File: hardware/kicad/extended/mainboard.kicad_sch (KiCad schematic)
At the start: 83 parts, among them J1 XT60PB-M vertical, J10 Body NeoPixel, J11 Slip ring (body lights), J13 SPK L, J14 SPK R, J15 ESTOP, J17 I2C-B exp (RP2350), J2 DFR0601 ribbon 2x5, J3 DFR0601 ribbon 2x5, J4 Servo L, J5 Servo R, J6 IMU BMI160 I2C, J7 S2S AS5600/pot, J8 Dome encoder, J9 Hall, Q1 Si7461DP P-FET RPP, U3 DFPlayer Mini, U5 AP7361C-33 3.3V LDO, U6 74AHCT125, U7 74LVC245A

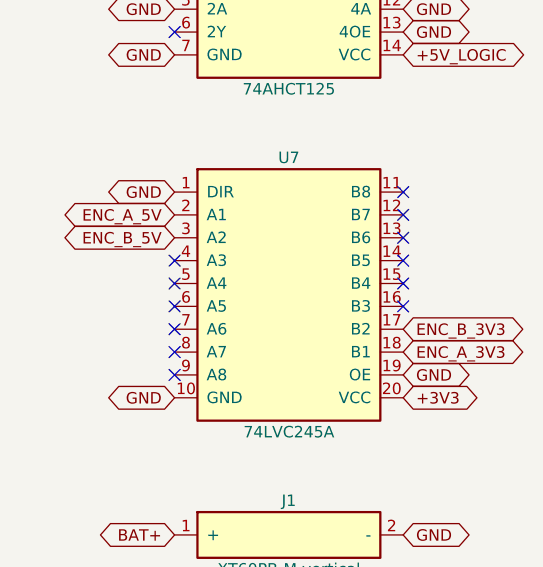
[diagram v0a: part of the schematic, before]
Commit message: v10 mainboard r7: fix U7 74LVC245 direction (DIR -> +3V3, A->B), tie unused A3..A8 to GND
DIR was strapped to GND, which per the SN74LVC245A pin table is B->A: the 5 V dome
encoder on A1/A2 would never reach the RP2350 on B1/B2 and U7's A outputs would fight
the encoder. Pad 1 is now +3V3 via a 0.2 mm jumper around the package end to pin 20;
A3..A8 (inputs once DIR=H) run along the row to pin 10 GND. Compact board still
0 DRC errors (17 warnings, 2 cosmetic zone-island lines). Extended board synced.
Regenerated both schematics (compact's was stale) and the JLCPCB package
(ZDrive_v10_compact_*_r7.zip; BOM/CPL unchanged from the r6 upload).

Rev-A boards built from r6 gerbers: cut the GND spoke into U7 pin 1 and bridge pin 1
to pin 20.

Co-Authored-By: Claude Fable 5 <noreply@anthropic.com>
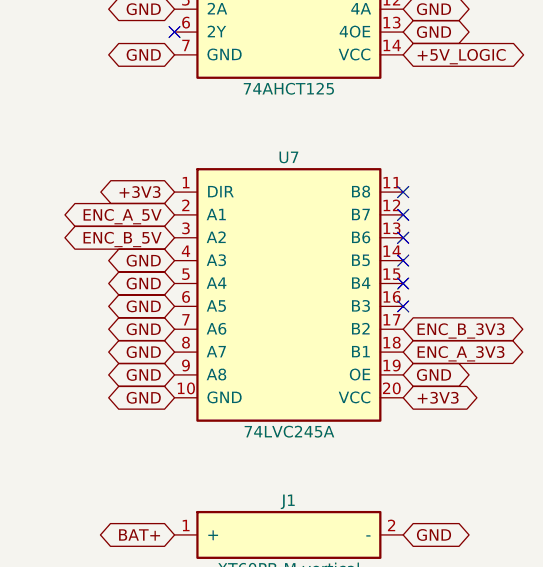
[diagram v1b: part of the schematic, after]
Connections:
- net +3V3: now also U7.1 (DIR)
- net GND: now also U7.4 (A3), U7.5 (A4), U7.6 (A5), U7.7 (A6), U7.8 (A7), U7.9 (A8); no longer U7.1 (DIR)
- no-connect marks 39 -> 33
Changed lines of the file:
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@@
     (instances (project "mainboard" (path "/0b82c761-6368-5a59-877e-dce7a78c7d89" (reference "U7") (unit 1))))
   )
-  (global_label "GND" (shape bidirectional) (at 59.69 207.01 180) (fields_autoplaced yes) (effects (font (size 1.27 1.27)) (justify right)) (property "Intersheetrefs" "${INTERSHEET_REFS}" (at 59.69 207.01 0) (effects (font (size 1.27 1.27)) (hide yes))))
+  (global_label "+3V3" (shape bidirectional) (at 59.69 207.01 180) (fields_autoplaced yes) (effects (font (size 1.27 1.27)) (justify right)) (property "Intersheetrefs" "${INTERSHEET_REFS}" (at 59.69 207.01 0) (effects (font (size 1.27 1.27)) (hide yes))))
   (global_label "ENC_A_5V" (shape bidirectional) (at 59.69 209.55 180) (fields_autoplaced yes) (effects (font (size 1.27 1.27)) (justify right)) (property "Intersheetrefs" "${INTERSHEET_REFS}" (at 59.69 209.55 0) (effects (font (size 1.27 1.27)) (hide yes))))
   (global_label "ENC_B_5V" (shape bidirectional) (at 59.69 212.09 180) (fields_autoplaced yes) (effects (font (size 1.27 1.27)) (justify right)) (property "Intersheetrefs" "${INTERSHEET_REFS}" (at 59.69 212.09 0) (effects (font (size 1.27 1.27)) (hide yes))))
-  (no_connect (at 59.69 214.63))
-  (no_connect (at 59.69 217.17))
-  (no_connect (at 59.69 219.71))
-  (no_connect (at 59.69 222.25))
-  (no_connect (at 59.69 224.79))
-  (no_connect (at 59.69 227.33))
+  (global_label "GND" (shape bidirectional) (at 59.69 214.63 180) (fields_autoplaced yes) (effects (font (size 1.27 1.27)) (justify right)) (property "Intersheetrefs" "${INTERSHEET_REFS}" (at 59.69 214.63 0) (effects (font (size 1.27 1.27)) (hide yes))))
+  (global_label "GND" (shape bidirectional) (at 59.69 217.17 180) (fields_autoplaced yes) (effects (font (size 1.27 1.27)) (justify right)) (property "Intersheetrefs" "${INTERSHEET_REFS}" (at 59.69 217.17 0) (effects (font (size 1.27 1.27)) (hide yes))))
+  (global_label "GND" (shape bidirectional) (at 59.69 219.71 180) (fields_autoplaced yes) (effects (font (size 1.27 1.27)) (justify right)) (property "Intersheetrefs" "${INTERSHEET_REFS}" (at 59.69 219.71 0) (effects (font (size 1.27 1.27)) (hide yes))))
+  (global_label "GND" (shape bidirectional) (at 59.69 222.25 180) (fields_autoplaced yes) (effects (font (size 1.27 1.27)) (justify right)) (property "Intersheetrefs" "${INTERSHEET_REFS}" (at 59.69 222.25 0) (effects (font (size 1.27 1.27)) (hide yes))))
+  (global_label "GND" (shape bidirectional) (at 59.69 224.79 180) (fields_autoplaced yes) (effects (font (size 1.27 1.27)) (justify right)) (property "Intersheetrefs" "${INTERSHEET_REFS}" (at 59.69 224.79 0) (effects (font (size 1.27 1.27)) (hide yes))))
+  (global_label "GND" (shape bidirectional) (at 59.69 227.33 180) (fields_autoplaced yes) (effects (font (size 1.27 1.27)) (justify right)) (property "Intersheetrefs" "${INTERSHEET_REFS}" (at 59.69 227.33 0) (effects (font (size 1.27 1.27)) (hide yes))))
   (global_label "GND" (shape bidirectional) (at 59.69 229.87 180) (fields_autoplaced yes) (effects (font (size 1.27 1.27)) (justify right)) (property "Intersheetrefs" "${INTERSHEET_REFS}" (at 59.69 229.87 0) (effects (font (size 1.27 1.27)) (hide yes))))
   (no_connect (at 85.09 207.01))
